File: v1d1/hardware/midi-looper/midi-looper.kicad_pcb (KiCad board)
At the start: 2 copper layers, 34 parts, among them J1 SW1, J10 Conn_01x05_Female, J11 MIDI IN 1 - Bk:M5 R:M4, J12 MIDI IN 2 - Bk:M5 R:M4, J13 MIDI IN 3 - Bk:M5 R:M4, J2 SW2, J3 SW3, J4 Batt IN, J5 SSD1306 SPI, J6 MIDI OUT 1 -Y:M5 R:M4, J7 MIDI OUT 2 -Y:M5 R:M4, J8 MIDI OUT 3 -Y:M5 R:M4, J9 Rot. Enc. Bk/Or:GND - Re:A - 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, SW1 Rotary_Encoder_Switch, U1 6N138, U2 Teensy3.2_breadboard_friendly, U3 6N138, U4 6N138

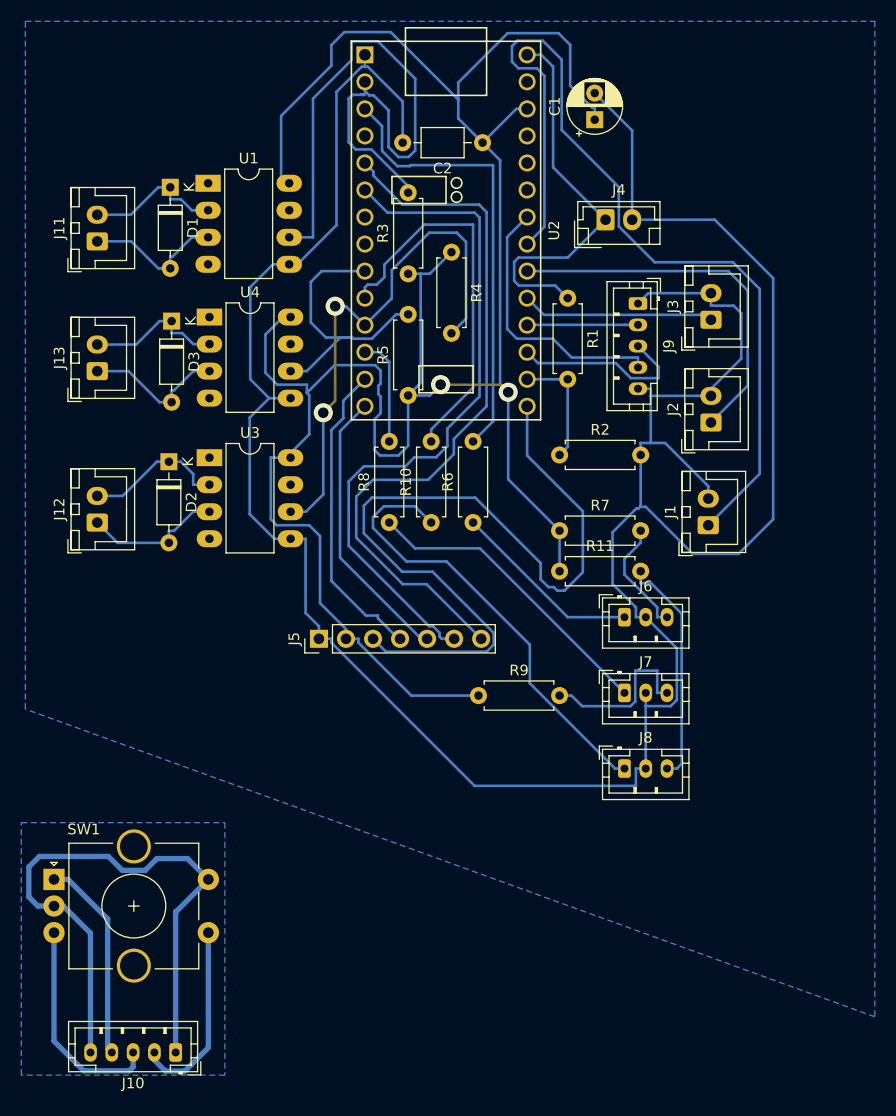
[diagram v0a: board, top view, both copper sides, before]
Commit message: Finalized compact version
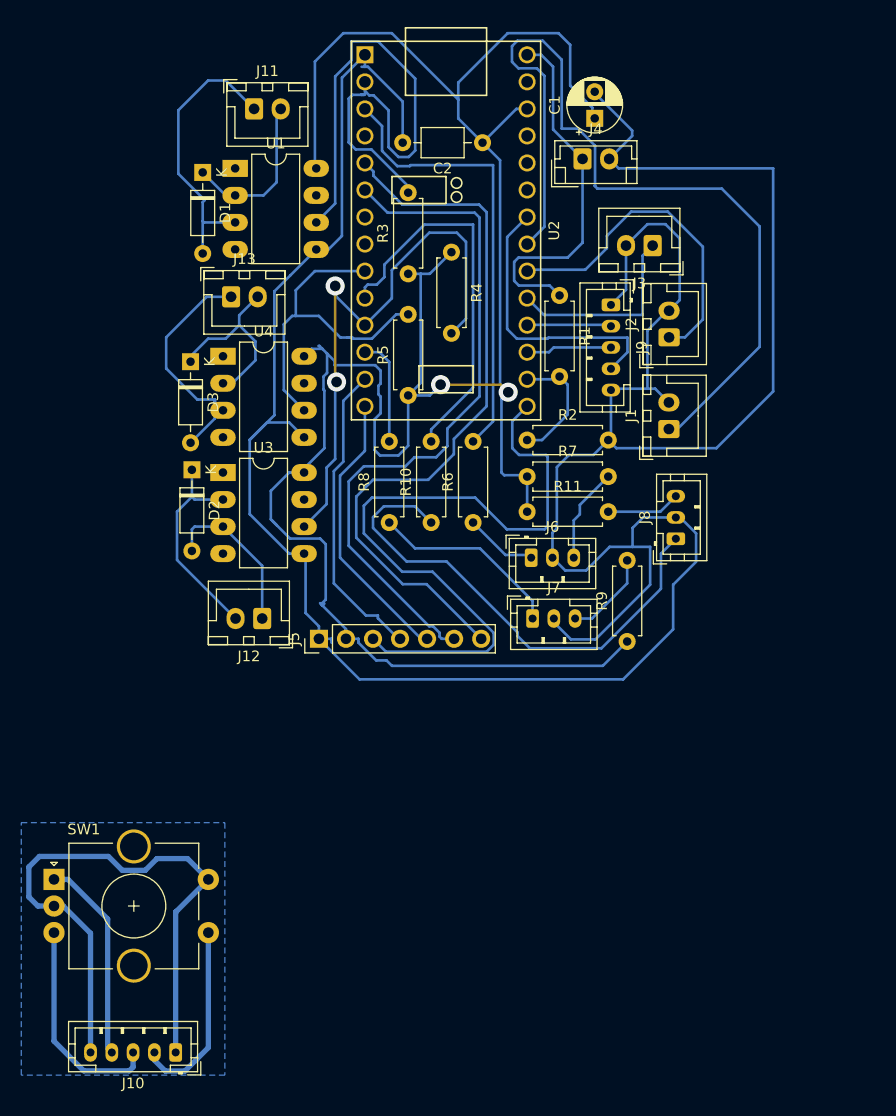
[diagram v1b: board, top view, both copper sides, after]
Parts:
- moved J8 22.1 mm to (112.0, 85.1), turned to 90 degrees
- moved J11 19.3 mm to (72.4, 44.7), turned to 0 degrees
- moved J12 17.9 mm to (73.2, 92.6), turned to 180 degrees
- moved R9 14.9 mm to (107.4, 94.7), turned to 90 degrees
- moved J13 14.4 mm to (70.2, 62.4), turned to 0 degrees
- moved J7 11.1 mm to (98.6, 92.6)
- moved J6 10.4 mm to (98.4, 86.9)
- moved J1 9.77 mm to (111.4, 74.8)
- moved J2 8.92 mm to (111.4, 66.2)
- moved J3 8.87 mm to (109.8, 57.5), turned to 180 degrees
- moved R11 6.37 mm to (98.0, 82.5)
- moved J4 6.11 mm to (103.3, 49.4)
- moved R7 5.92 mm to (98.0, 79.2)
- moved D3 4.20 mm to (66.4, 68.5)
- moved U4 3.90 mm to (69.5, 67.9)
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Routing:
- net GND: track 263.6 -> 280.8 mm
- net Net-(J8-Pad3): track 21.8 -> 6.95 mm
- net Net-(D1-Pad2): track 13.3 -> 27.0 mm
- net Net-(J6-Pad1): track 17.9 -> 6.83 mm
- net Net-(J7-Pad1): track 28.7 -> 18.2 mm
- net Net-(J5-Pad3): track 75.8 -> 65.5 mm
- net Net-(J9-Pad3): track 17.2 -> 8.06 mm
- net Net-(D3-Pad2): track 13.6 -> 22.7 mm
- net Net-(J7-Pad3): track 15.7 -> 8.42 mm
- net Net-(D2-Pad1): track 13.4 -> 20.4 mm
- net /RX3: track 27.1 -> 32.8 mm
- net Net-(D3-Pad1): track 13.0 -> 17.7 mm
- net Net-(J8-Pad1): track 42.6 -> 47.0 mm
- net /RX1: track 61.0 -> 57.3 mm
- net Net-(J2-Pad1): track 35.3 -> 31.6 mm
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- removed copper zone on B.Cu, net GND
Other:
- net class Default removed
- net class Easy removed
